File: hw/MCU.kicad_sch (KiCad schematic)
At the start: 15 parts, among them J2 Conn_01x06, SW2 SKRPACE010, SW3 SKRPACE010, U2 N32L406RBL7

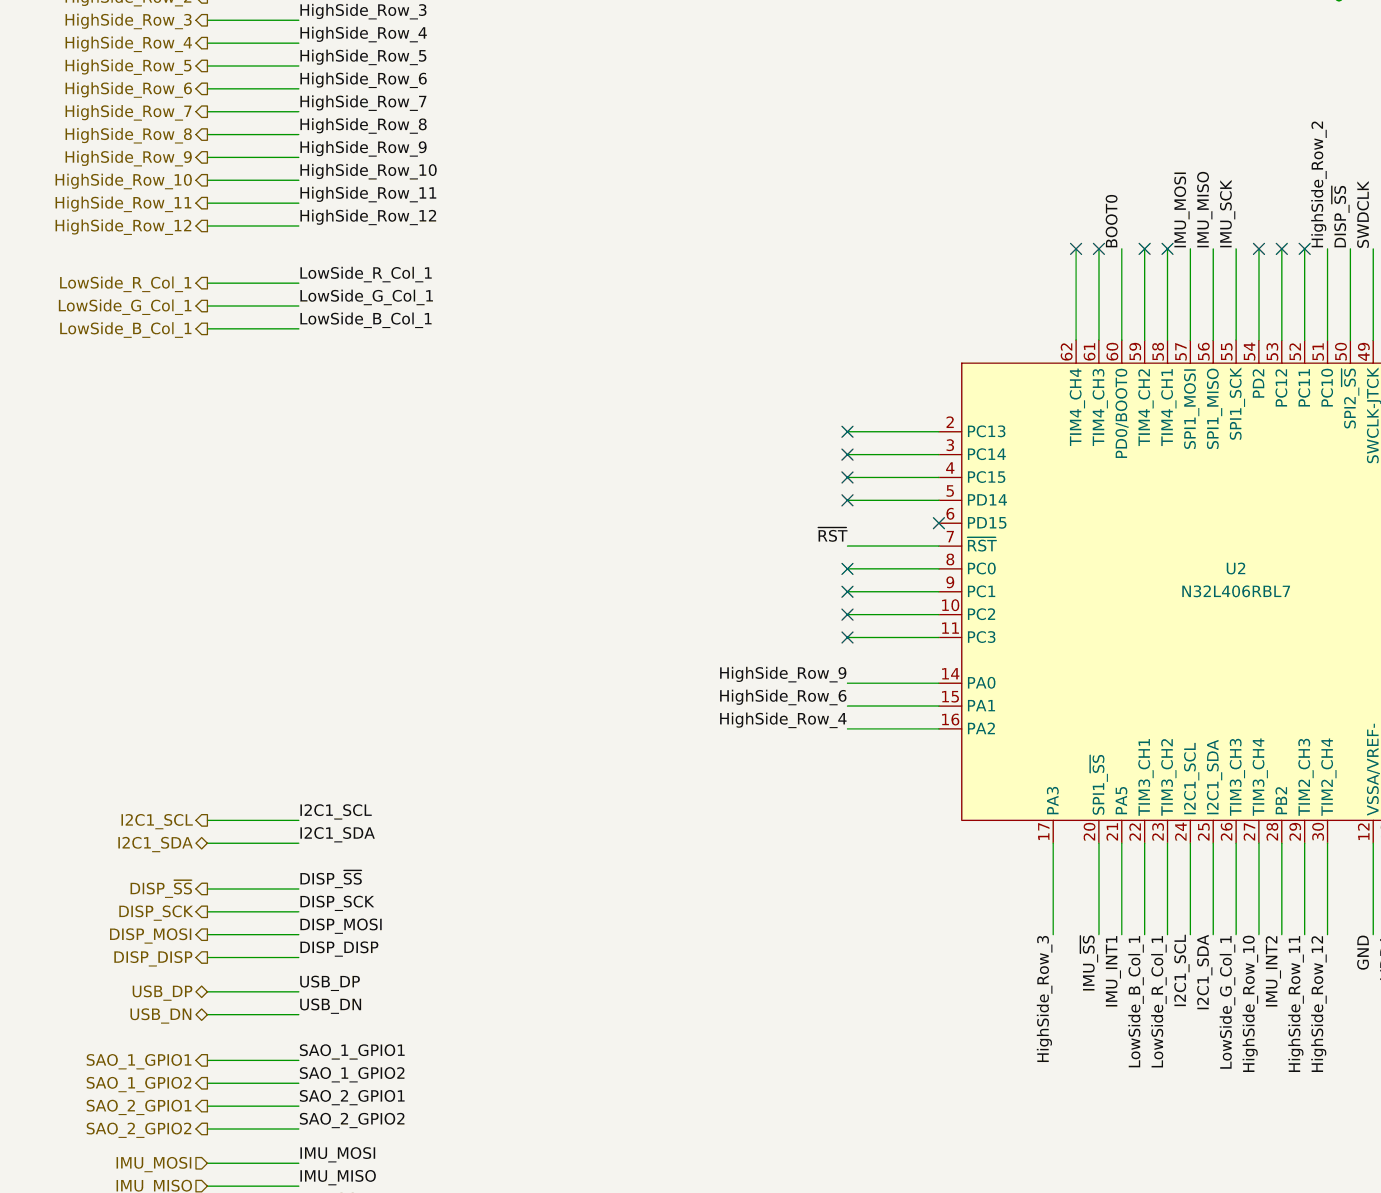
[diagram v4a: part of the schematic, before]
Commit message: routed SAO I2C
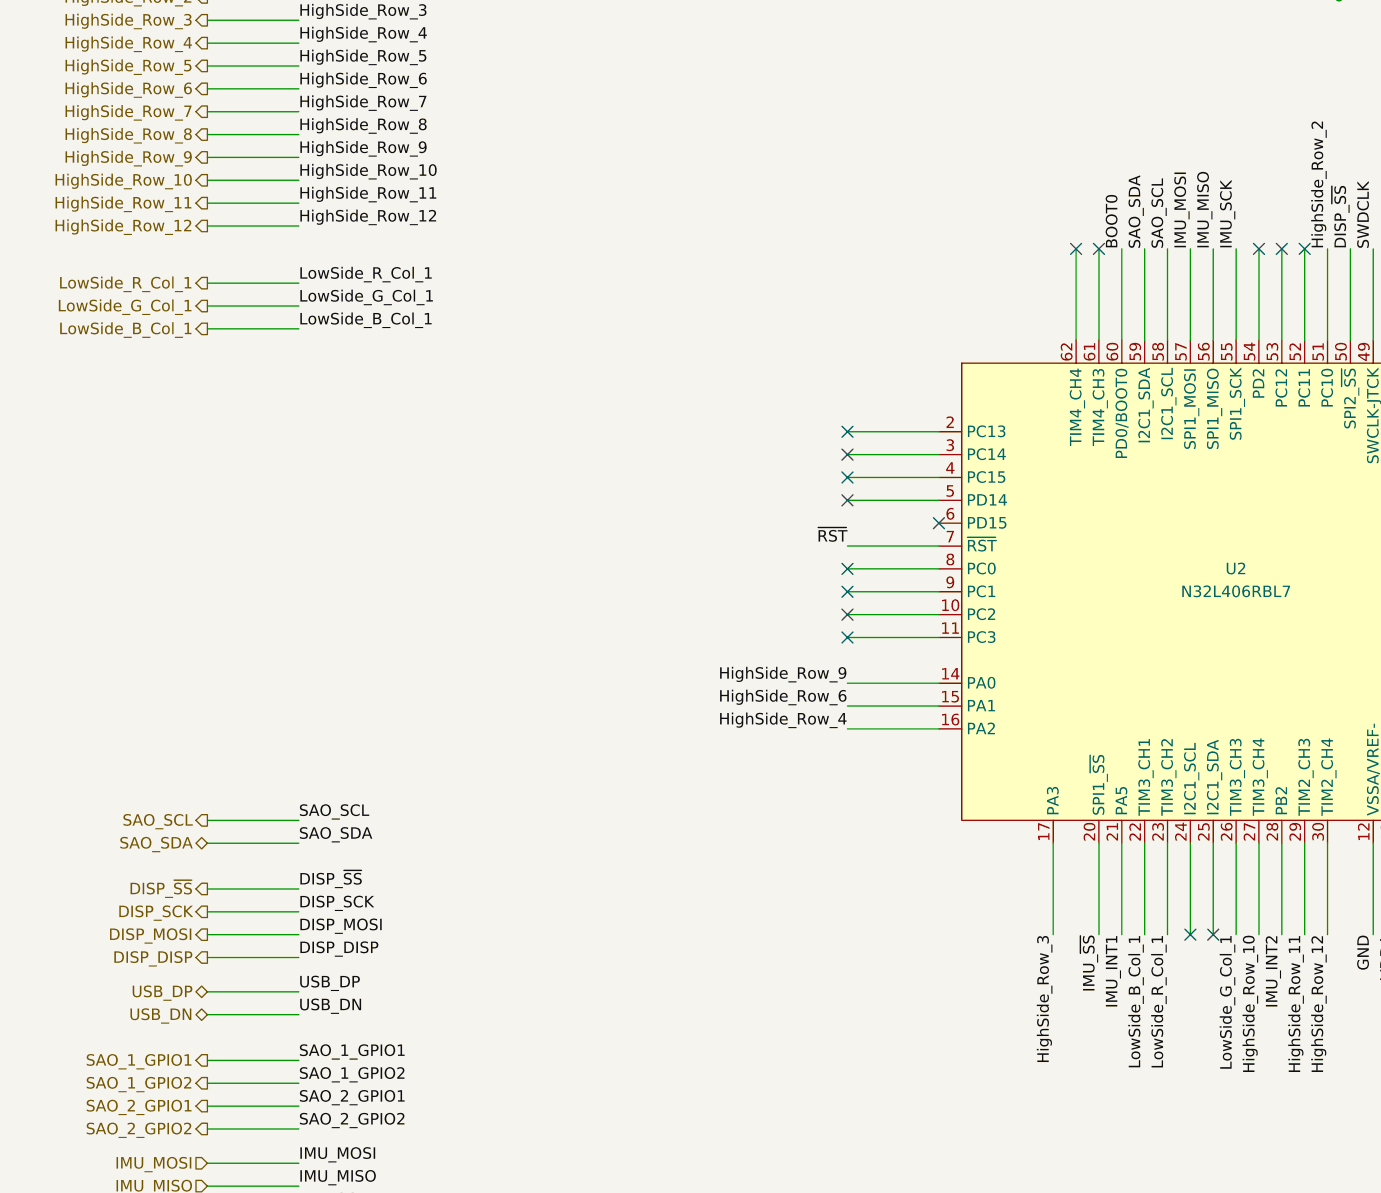
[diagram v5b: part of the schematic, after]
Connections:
- net SAO_SCL: now reaches U2.58 (PB6)
- net SAO_SDA: now reaches U2.59 (PB7)
- net I2C1_SCL: no longer names the net of U2.24 (PC4)
- net I2C1_SDA: no longer names the net of U2.25 (PC5)
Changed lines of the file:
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@@
   (no_connect (at 114.3 101.6))
   (no_connect (at 162.56 60.96))
+  (no_connect (at 154.94 137.16))
+  (no_connect (at 152.4 137.16))
   (no_connect (at 114.3 86.36))
   (no_connect (at 139.7 60.96))
@@
   (no_connect (at 160.02 60.96))
   (no_connect (at 114.3 81.28))
-  (no_connect (at 149.86 60.96))
   (no_connect (at 182.88 127))
-  (no_connect (at 147.32 60.96))
   (no_connect (at 124.46 91.44))
   (no_connect (at 114.3 104.14))
@@
     (effects (font (size 1.27 1.27)) (justify left bottom))
   )
-  (label "I2C1_SDA" (at 154.94 137.16 270) (fields_autoplaced)
-    (effects (font (size 1.27 1.27)) (justify right bottom))
+  (label "SAO_SDA" (at 147.32 60.96 90) (fields_autoplaced)
+    (effects (font (size 1.27 1.27)) (justify left bottom))
   )
   (label "~{RST}" (at 114.3 93.98 180) (fields_autoplaced)
@@
     (effects (font (size 1.27 1.27)) (justify left bottom))
   )
-  (label "I2C1_SCL" (at 152.4 137.16 270) (fields_autoplaced)
-    (effects (font (size 1.27 1.27)) (justify right bottom))
+  (label "SAO_SCL" (at 149.86 60.96 90) (fields_autoplaced)
+    (effects (font (size 1.27 1.27)) (justify left bottom))
   )
   (label "SAO_2_GPIO1" (at 200.66 88.9 0) (fields_autoplaced)
@@
     (effects (font (size 1.27 1.27)) (justify right bottom))
   )
-  (label "I2C1_SCL" (at 53.34 124.46 0) (fields_autoplaced)
+  (label "SAO_SCL" (at 53.34 124.46 0) (fields_autoplaced)
     (effects (font (size 1.27 1.27)) (justify left bottom))
   )
@@
     (effects (font (size 1.27 1.27)) (justify right bottom))
   )
-  (label "I2C1_SDA" (at 53.34 127 0) (fields_autoplaced)
+  (label "SAO_SDA" (at 53.34 127 0) (fields_autoplaced)
     (effects (font (size 1.27 1.27)) (justify left bottom))
   )
@@
     (effects (font (size 1.27 1.27)) (justify right))
   )
-  (hierarchical_label "I2C1_SDA" (shape bidirectional) (at 43.18 127 180) (fields_autoplaced)
+  (hierarchical_label "SAO_SDA" (shape bidirectional) (at 43.18 127 180) (fields_autoplaced)
     (effects (font (size 1.27 1.27)) (justify right))
   )
@@
     (effects (font (size 1.27 1.27)) (justify right))
   )
-  (hierarchical_label "I2C1_SCL" (shape output) (at 43.18 124.46 180) (fields_autoplaced)
+  (hierarchical_label "SAO_SCL" (shape output) (at 43.18 124.46 180) (fields_autoplaced)
     (effects (font (size 1.27 1.27)) (justify right))
   )
@@
     (pin "56" (alternate "SPI1_MISO"))
     (pin "57" (alternate "SPI1_MOSI"))
-    (pin "58" (alternate "TIM4_CH1"))
-    (pin "59" (alternate "TIM4_CH2"))
+    (pin "58" (alternate "I2C1_SCL"))
+    (pin "59" (alternate "I2C1_SDA"))
     (pin "6")
     (pin "60")

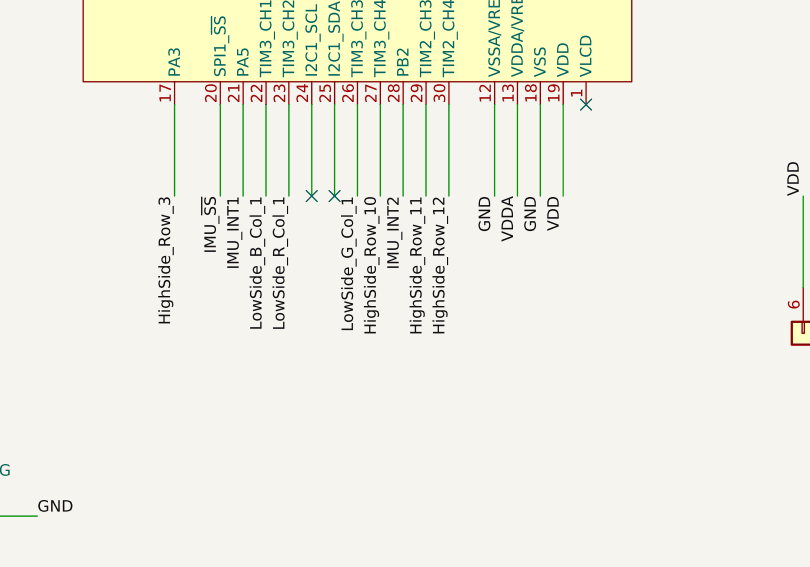
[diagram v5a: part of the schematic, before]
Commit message: change routing high side
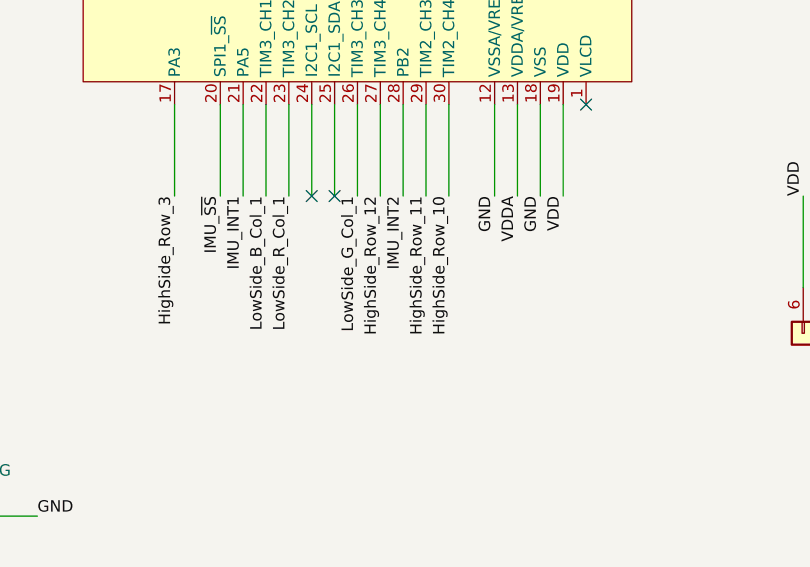
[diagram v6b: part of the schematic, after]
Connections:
- net HighSide_Row_10: now also U2.30 (PB11); no longer U2.27 (PB1)
- net HighSide_Row_12: now also U2.27 (PB1); no longer U2.30 (PB11)
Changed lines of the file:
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@@
     (effects (font (size 1.27 1.27)) (justify left bottom))
   )
-  (label "HighSide_Row_12" (at 167.64 137.16 270) (fields_autoplaced)
+  (label "HighSide_Row_12" (at 160.02 137.16 270) (fields_autoplaced)
     (effects (font (size 1.27 1.27)) (justify right bottom))
   )
@@
     (effects (font (size 1.27 1.27)) (justify right bottom))
   )
-  (label "HighSide_Row_10" (at 160.02 137.16 270) (fields_autoplaced)
+  (label "HighSide_Row_10" (at 167.64 137.16 270) (fields_autoplaced)
     (effects (font (size 1.27 1.27)) (justify right bottom))
   )
